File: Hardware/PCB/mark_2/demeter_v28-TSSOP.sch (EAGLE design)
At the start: 68 parts, among them IC1 4050, IC2 LM1117-5.0, IC3 LM1117-3.3, IC4 XBEE, IC5 MCP3424, IC6 MCP23017SO, IC8 ATMEGA32U4-AU, Q1 IRLML6402, Q2 IRLML6402, Q3 IRLML6402, Q4 IRLML6402, Q5 IRLML6402, Q6 IRLML6402, X2 POWER

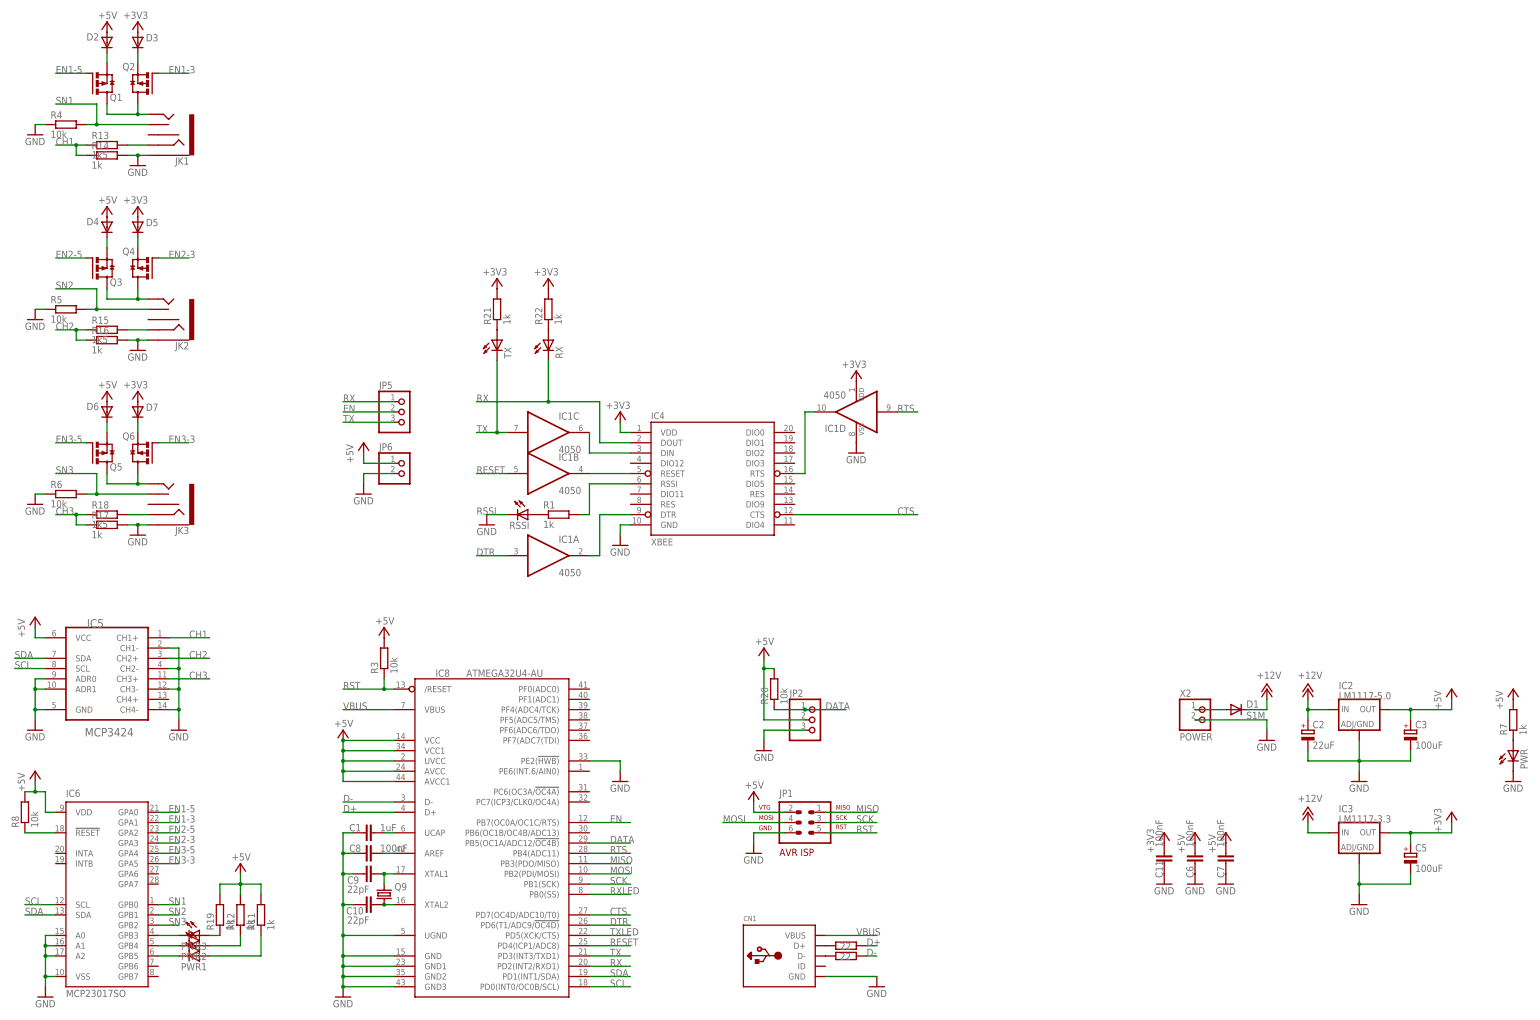
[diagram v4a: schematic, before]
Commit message: 
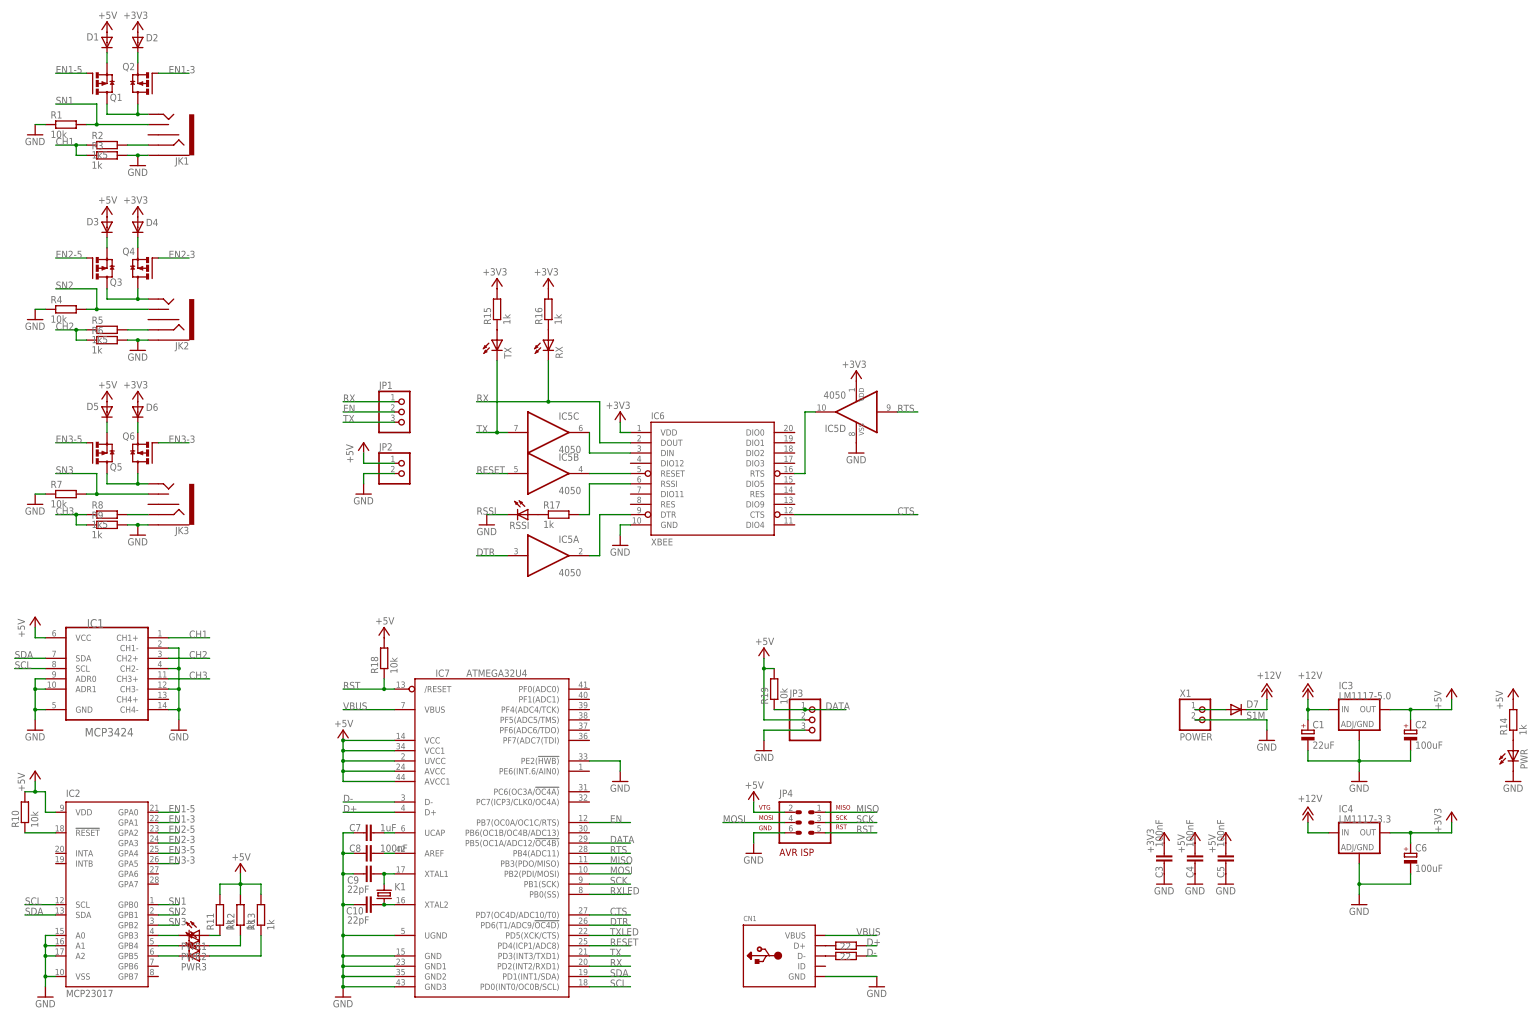
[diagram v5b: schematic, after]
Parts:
- removed C11: 100nF, mark_2:C-EUC0805K
- removed JP5: (no value), mark_2:PINHD-1X3180
- removed JP6: (no value), mark_2:PINHD-1X2
- removed R22: 1k, mark_2:R-EU_R0805
- added C4: 100nF, mark_2:C-EUC0805K
- added JP3: (no value), mark_2:PINHD-1X3180
- added JP4: AVR-ISP, mark_2:AVR-ISP-6
- added R2: 1k5, mark_2:R-EU_R0805
- C1: value 1uF -> 22uF; device mark_2:C-EUC0805K -> mark_2:CPOL-EUPD
- C2: value 22uF -> 100uF
- C3, C5: value 100uF -> 100nF; device mark_2:CPOL-EUPD -> mark_2:C-EUC0805K
- C6: value 100nF -> 100uF; device mark_2:C-EUC0805K -> mark_2:CPOL-EUPD
- C7: value 100nF -> 1uF
- D1: value S1M -> MBR0520; device mark_2:S1M -> mark_2:MBR0520
- D7: value MBR0520 -> S1M; device mark_2:MBR0520 -> mark_2:S1M
- IC1: value 4050 -> MCP3424; device mark_2:4050D -> mark_2:MCP3424T
- IC2: value LM1117-5.0 -> MCP23017; device mark_2:LM1117DT -> mark_2:MCP23017SO
- IC3: value LM1117-3.3 -> LM1117-5.0
- IC4: value XBEE -> LM1117-3.3; device mark_2:XBEE-1B1 -> mark_2:LM1117DT
- IC5: value MCP3424 -> 4050; device mark_2:MCP3424T -> mark_2:4050D
- IC6: value MCP23017SO -> XBEE; device mark_2:MCP23017SO -> mark_2:XBEE-1B1
- IC7: value ATMEGA32U4-AU -> ATMEGA32U4
- JP1: value AVR-ISP -> (none); device mark_2:AVR-ISP-6 -> mark_2:PINHD-1X3180
- JP2: device mark_2:PINHD-1X3180 -> mark_2:PINHD-1X2
- R1, R19, R7: value 1k -> 10k
- R10: value 22 -> 10k
- R13, R15: value 1k5 -> 1k
- R18: value 1k5 -> 10k
- R20: value 10k -> 22
- R21: value 1k -> 22
- R3, R6: value 10k -> 1k
- R5, R8: value 10k -> 1k5
- R9: value 22 -> 1k
- renumbered IC8 to IC7, Q9 to K1, X2 to X1
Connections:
- removed net N$23 (its old number): PWR3.A, R19.1
- new net N$5: PWR3.A, R13.1
- net +12V: now also C1.+, D7.C, IC4.IN; no longer C2.+, D1.C, IC2.IN
- net +3V3: now also C3.1, C6.+, D2.A, D4.A, D6.A, IC4.OUT, IC5P.VDD, IC6.VDD, R15.2, R16.2; no longer C11.1, C5.+, D3.A, D5.A, D7.A, IC1P.VDD, IC3.OUT, IC4.VDD, R21.2, R22.2
- net +5V: now also C2.+, C4.1, C5.1, D1.A, D3.A, D5.A, IC1.VCC, IC2.VDD, IC3.OUT, JP2.1, JP3.2, JP4.VTG, R10.2, R13.2, R14.2, R18.2; no longer C3.+, C6.1, C7.1, D2.A, D4.A, D6.A, IC2.OUT, IC5.VCC, IC6.VDD, JP1.VTG, JP2.2, JP6.1, R20.2, R3.2, R7.2, R8.2
- net CH1: now also IC1.CH1+, R2.1, R3.1; no longer IC5.CH1+, R13.1, R14.1
- net CH2: now also IC1.CH2+, R5.1, R6.1; no longer IC5.CH2+, R15.1, R16.1
- net CH3: now also IC1.CH3+, R8.1, R9.1; no longer IC5.CH3+, R17.1, R18.1
- net CTS: now also IC6.CTS; no longer IC4.CTS
- net D+: now also R20.1; no longer R9.1
- net D-: now also R21.1; no longer R10.1
- net DATA: now also JP3.1, R19.1; no longer JP2.1, R20.1
- net DTR: now also IC5A.I; no longer IC1A.I
- net EN: now also JP1.2; no longer JP5.2
- net EN1-3: now also IC2.GPA1; no longer IC6.GPA1
- net EN1-5: now also IC2.GPA0; no longer IC6.GPA0
- net EN2-3: now also IC2.GPA3; no longer IC6.GPA3
- net EN2-5: now also IC2.GPA2; no longer IC6.GPA2
- net EN3-3: now also IC2.GPA5; no longer IC6.GPA5
- net EN3-5: now also IC2.GPA4; no longer IC6.GPA4
- net GND: now also C1.-, C3.2, C4.2, C5.2, C6.-, IC1.ADR0, IC1.ADR1, IC1.CH1-, IC1.CH2-, IC1.CH3-, IC1.CH4-, IC1.GND, IC2.A0, IC2.A1, IC2.A2, IC2.VSS, IC4.ADJ, IC5P.VSS, IC6.GND, JP2.2, JP3.3, JP4.GND, R1.1, R3.2, R6.2, R7.1, R9.2; no longer C1.2, C11.2, C3.-, C5.-, C6.2, IC1P.VSS, IC2.ADJ, IC4.GND, IC5.ADR0, IC5.ADR1, IC5.CH1-, IC5.CH2-, IC5.CH3-, IC5.CH4-, IC5.GND, IC6.A0, IC6.A1, IC6.A2, IC6.VSS, JP1.GND, JP2.3, JP6.2, R14.2, R16.2, R17.2, R5.1, R6.1
- net MISO: now also JP4.MISO; no longer JP1.MISO
- net MOSI: now also JP4.MOSI; no longer JP1.MOSI
- net N$1: now also D7.A; no longer D1.A
- net N$10: now also IC2.GPB3, PWR1.C; no longer IC6.GPB3, PWR3.C
- net N$11: now also IC2.!RESET, R10.1; no longer IC6.!RESET, R8.1
- net N$13: now also D1.C; no longer D2.C
- net N$14: now also D2.C; no longer D3.C
- net N$16: now also D3.C; no longer D4.C
- net N$17: now also D4.C; no longer D5.C
- net N$19: now also D5.C; no longer D6.C
- net N$2: now also R14.1; no longer R7.1
- net N$20: now also D6.C; no longer D7.C
- net N$24: now also C7.1; no longer C1.1
- net N$28: now also R20.2; no longer R9.2
- net N$29: now also R21.2; no longer R10.2
- net N$3: now also IC5C.O, IC6.DIN; no longer IC1C.O, IC4.DIN
- net N$30: now also R2.2; no longer R13.2
- net N$32: now also R5.2; no longer R15.2
- net N$33: now also IC2.GPB4; no longer IC6.GPB4
- net N$34: now also R8.2; no longer R18.2
- net N$36: now also R15.1; no longer R21.1
- net N$37: now also R16.1; no longer R22.1
- net N$4: now also IC5B.O, IC6.RESET; no longer IC1B.O, IC4.RESET
- net N$6: now also R17.1; no longer R1.1
- net N$7: now also IC5A.O, IC6.DTR; no longer IC1A.O, IC4.DTR
- net N$8: now also IC5D.O, IC6.RTS; no longer IC1D.O, IC4.RTS
- net N$9: now also IC2.GPB5, PWR3.C; no longer IC6.GPB5, PWR1.C
- net RESET: now also IC5B.I; no longer IC1B.I
- net RSSI: now also IC6.RSSI, R17.2; no longer IC4.RSSI, R1.2
- net RST: now also JP4.RST, R18.1; no longer JP1.RST, R3.1
- net RTS: now also IC5D.I; no longer IC1D.I
- net RX: now also IC6.DOUT, JP1.1; no longer IC4.DOUT, JP5.1
- net SCK: now also JP4.SCK; no longer JP1.SCK
- net SCL: now also IC1.SCL, IC2.SCL; no longer IC5.SCL, IC6.SCL
- net SDA: now also IC1.SDA, IC2.SDA; no longer IC5.SDA, IC6.SDA
- net SN1: now also IC2.GPB0, R1.2; no longer IC6.GPB0, R4.2
- net SN2: now also IC2.GPB1, R4.2; no longer IC6.GPB1, R5.2
- net SN3: now also IC2.GPB2, R7.2; no longer IC6.GPB2, R6.2
- net TX: now also IC5C.I, JP1.3; no longer IC1C.I, JP5.3
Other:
- moved on the sheet: C2, C7, D2, D3, D4, D5, D6, IC3, PWR1, PWR3, R1, R11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
